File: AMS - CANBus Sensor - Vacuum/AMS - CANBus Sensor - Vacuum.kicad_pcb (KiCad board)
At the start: 2 copper layers, 72.9 x 71.1 mm, 45 parts, among them IC2 OPA4340UA, J1 Power_And_CAN, J2 Power_And_CAN, J3 TTL_Programmer, J4 ICSP, J5 Conn_01x02, J6 Screw_Terminal_01x02, Q1 IRF9Z34NPBF, U1 3568, U2 ATmega328P-P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

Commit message: wip for the vacuum
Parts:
- removed J2: Power_And_CAN, TerminalBlock_Phoenix:TerminalBlock_Phoenix_MPT-0,5-4-2.54_1x04_P2.54mm_Horizontal
- removed J6: Screw_Terminal_01x02, TerminalBlock_Phoenix:TerminalBlock_Phoenix_MPT-0,5-2-2.54_1x02_P2.54mm_Horizontal
- removed R12, R13: 47K, Resistor_SMD:R_1206_3216Metric_Pad1.30x1.75mm_HandSolder
- removed R14, R15, R8: 100K, Resistor_SMD:R_1206_3216Metric_Pad1.30x1.75mm_HandSolder
- removed RV1, RV2, RV3, RV4: 200k, Potentiometer_THT:Potentiometer_Bourns_3296W_Vertical
- IC2: value OPA4340UA -> MCP1804T-A002I_OT; footprint SamacSys_Parts:SOIC127P600X175-14N -> SamacSys_Parts:SOT95P270X145-5N
- R9: value 100K -> 1k; footprint Resistor_SMD:R_1206_3216Metric_Pad1.30x1.75mm_HandSolder -> Resistor_SMD:R_0603_1608Metric
- U1: value 3568 -> TL431LP; footprint SamacSys_Parts:3568 -> Package_TO_SOT_THT:TO-92_Inline
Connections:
- IC2 pad 1: /BareMinAtmel328P/PC1-A1 -> +VDC
- IC2 pad 2: /BareMinAtmel328P/PC1-A1 -> GND
- IC2 pad 3: /BufferedADC/ADCIN1 -> unconnected-(IC2-NC-Pad3)
- IC2 pad 4: +5V -> +VDC
- IC2 pad 5: /BufferedADC/ADCIN2 -> +10V
- R9 pad 1: GND -> +5V
- R9 pad 2: /BufferedADC/ADCIN2 -> +2V5
- U1 pad 1: Net-(J6-Pin_2) -> +2V5
- U1 pad 2: Net-(J6-Pin_1) -> GND
- U1 pad 3: +5V -> +2V5
- U2 pad 24: /BareMinAtmel328P/PC1-A1 -> +2V5
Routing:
- net GND: track 276.6 -> 0.00 mm, vias 2 -> 0
- net +5V: track 185.4 -> 0.00 mm, vias 2 -> 0
- net /BufferedADC/ADCIN4: track 98.9 -> 0.00 mm, vias 1 -> 0
- net /BareMinAtmel328P/PB3-D11-MOSI: track 98.5 -> 0.00 mm, vias 1 -> 0
- net /BareMinAtmel328P/PB1-D9: track 92.8 -> 0.00 mm, vias 2 -> 0
- net /BareMinAtmel328P/RESET: track 92.4 -> 0.00 mm, vias 4 -> 0
- net /BareMinAtmel328P/PC3-A3: track 78.5 -> 0.00 mm, vias 2 -> 0
- net Net-(U3-OSC1): track 77.0 -> 0.00 mm
- net /BareMinAtmel328P/PB5-D13-SCK: track 75.2 -> 0.00 mm, vias 2 -> 0
- net Net-(U3-OSC2): track 72.5 -> 0.00 mm
- net /BufferedADC/ADCIN3: track 58.3 -> 0.00 mm, vias 1 -> 0
- net /BareMinAtmel328P/PB4-D12-MISO: track 53.7 -> 0.00 mm, vias 2 -> 0
- net /BareMinAtmel328P/PC1-A1: track 51.2 -> 0.00 mm, vias 2 -> 0
- net /BareMinAtmel328P/PC2-A2: track 46.0 -> 0.00 mm, vias 3 -> 0
- net /BufferedADC/ADCIN2: track 45.2 -> 0.00 mm, vias 2 -> 0
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
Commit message: i think the Vacuum sensor is done i need to test s afew things and then this is ready for fab
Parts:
- removed R10, R11: 47K, Resistor_SMD:R_1206_3216Metric_Pad1.30x1.75mm_HandSolder
- added IC1: OPA2340UA_2K5, SamacSys_Parts:SOIC127P600X175-8N, B.Cu at (121.3, 102.7)
- added IC3: ADS1115IDGST, SamacSys_Parts:SOP50P490X110-10N, B.Cu at (153.9, 93.6)
- added IC4: 24PCDFA6D, SamacSys_Parts:24PCDFA6D, F.Cu at (159.3, 88.8)
- added IC6: 24PCDFA6D, SamacSys_Parts:24PCDFA6D, F.Cu at (159.3, 103.6)
- added IC8: INA849DR, SamacSys_Parts:SOIC127P600X175-8N, B.Cu at (167.4, 84.9)
- added IC9: INA849DR, SamacSys_Parts:SOIC127P600X175-8N, B.Cu at (167.6, 99.8)
- added R12: 10k, Resistor_SMD:R_1206_3216Metric_Pad1.30x1.75mm_HandSolder, B.Cu at (144.8, 86.9)
- added R13: 10k, Resistor_SMD:R_1206_3216Metric_Pad1.30x1.75mm_HandSolder, B.Cu at (144.8, 83.3)
- added R14: YR1B665RCC, SamacSys_Parts:RESAD1550W60L630D230, F.Cu at (163.0, 79.6)
- added R15: YR1B665RCC, SamacSys_Parts:RESAD1550W60L630D230, F.Cu at (163.0, 105.7)
- added R16: 120k, Resistor_SMD:R_1206_3216Metric_Pad1.30x1.75mm_HandSolder, F.Cu at (124.0, 101.5)
- added R17: 15k, Resistor_SMD:R_1206_3216Metric_Pad1.30x1.75mm_HandSolder, F.Cu at (129.1, 101.4)
- added R18: 47k, Resistor_SMD:R_1206_3216Metric_Pad1.30x1.75mm_HandSolder, F.Cu at (117.1, 101.8)
- added R19: 1M, Resistor_SMD:R_1206_3216Metric_Pad1.30x1.75mm_HandSolder, F.Cu at (117.1, 105.5)
- added R8: 10k, Resistor_SMD:R_1206_3216Metric_Pad1.30x1.75mm_HandSolder, B.Cu at (163.3, 92.6)
- moved R6 33.3 mm to (138.2, 59.5), turned to -90 degrees
- moved U4 24.5 mm to (143.9, 60.9), turned to -90 degrees
- moved J5 18.3 mm to (157.3, 62.6)
- moved R7 18.3 mm to (157.4, 59.1)
- moved D1 14.2 mm to (169.3, 70.1), turned to 0 degrees
- moved U1 13.7 mm to (169.8, 111.6)
- moved Q1 12.8 mm to (142.7, 73.2)
- moved R5 10.8 mm to (135.5, 80.1)
- moved U3 6.09 mm to (151.8, 73.7)
- moved J4 6.01 mm to (151.8, 71.1)
- moved J1 5.72 mm to (161.9, 75.1)
- moved C2 2.19 mm to (154.2, 115.6)
- moved C3 2.19 mm to (154.2, 115.6)
- moved C4 2.19 mm to (159.6, 115.5)
- moved Y1 2.19 mm to (154.6, 119.7)
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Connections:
- U2 pad 24: +2V5 -> /BareMinAtmel328P/PC1-A1
- U2 pad 27: /BareMinAtmel328P/PC4-A4-SDA -> /SDAB
- U2 pad 28: /BareMinAtmel328P/PC5-A5-SCL -> /SCLB
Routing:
- net GND: track 0.00 -> 284.1 mm, vias 0 -> 2
- net +5V: track 0.00 -> 194.1 mm, vias 0 -> 4
- net /ADS1115/AIN0: track 0.00 -> 83.4 mm, vias 0 -> 3
- net /BareMinAtmel328P/RESET: track 0.00 -> 66.6 mm, vias 0 -> 2
- net +10V: track 0.00 -> 59.3 mm, vias 0 -> 1
- net +2V5: track 0.00 -> 57.9 mm, vias 0 -> 1
- net /BareMinAtmel328P/PB1-D9: track 0.00 -> 52.2 mm, vias 0 -> 2
- net /BareMinAtmel328P/PB4-D12-MISO: track 0.00 -> 48.8 mm, vias 0 -> 3
- net /BareMinAtmel328P/PB3-D11-MOSI: track 0.00 -> 48.2 mm, vias 0 -> 3
- net /ADS1115/AIN3: track 0.00 -> 46.0 mm, vias 0 -> 2
- net +VDC: track 0.00 -> 45.3 mm, vias 0 -> 2
- net Net-(U3-OSC2): track 0.00 -> 44.2 mm, vias 0 -> 3
- net Net-(U3-OSC1): track 0.00 -> 43.5 mm, vias 0 -> 2
- net /BareMinAtmel328P/PB5-D13-SCK: track 0.00 -> 43.3 mm, vias 0 -> 3
- net /BareMinAtmel328P/PD1-TX: track 0.00 -> 39.9 mm
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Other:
- board text added: "AMS CANBus Vacuum V1.0 Rev A"
- board text added: "PORT1"
- board text added: "PORT2"
- board text removed: "1 Amp 5V"
- board text removed: "ADC"
- board text removed: "AMS CANBus Voltage V1.0 Rev A"
- board text removed: "Fused"
- board text removed: "In"
- board text removed: "In 1"
- board text removed: "In 2"
- board text removed: "In 3"
- board text removed: "In 4"

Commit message: vacuum wip
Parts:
- added C10: 22nF, Capacitor_SMD:C_1206_3216Metric_Pad1.33x1.80mm_HandSolder, B.Cu at (169.6, 108.3)
- added C11: 1uF, Capacitor_SMD:C_0603_1608Metric_Pad1.08x0.95mm_HandSolder, B.Cu at (124.9, 97.3)
- added C8: 10uF, Capacitor_SMD:C_0603_1608Metric_Pad1.08x0.95mm_HandSolder, B.Cu at (122.0, 89.8)
- added C9: 22uF, Capacitor_SMD:C_0603_1608Metric_Pad1.08x0.95mm_HandSolder, F.Cu at (126.1, 89.8)
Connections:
- U2 pad 5: /BareMinAtmel328P/PD3-D3 -> /ADS1115/Alert/Ready
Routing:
- net GND: track 284.1 -> 298.3 mm
- net +2V5: track 57.9 -> 61.9 mm
- net +5V: track 194.1 -> 196.7 mm
- net +VDC: track 45.3 -> 47.0 mm

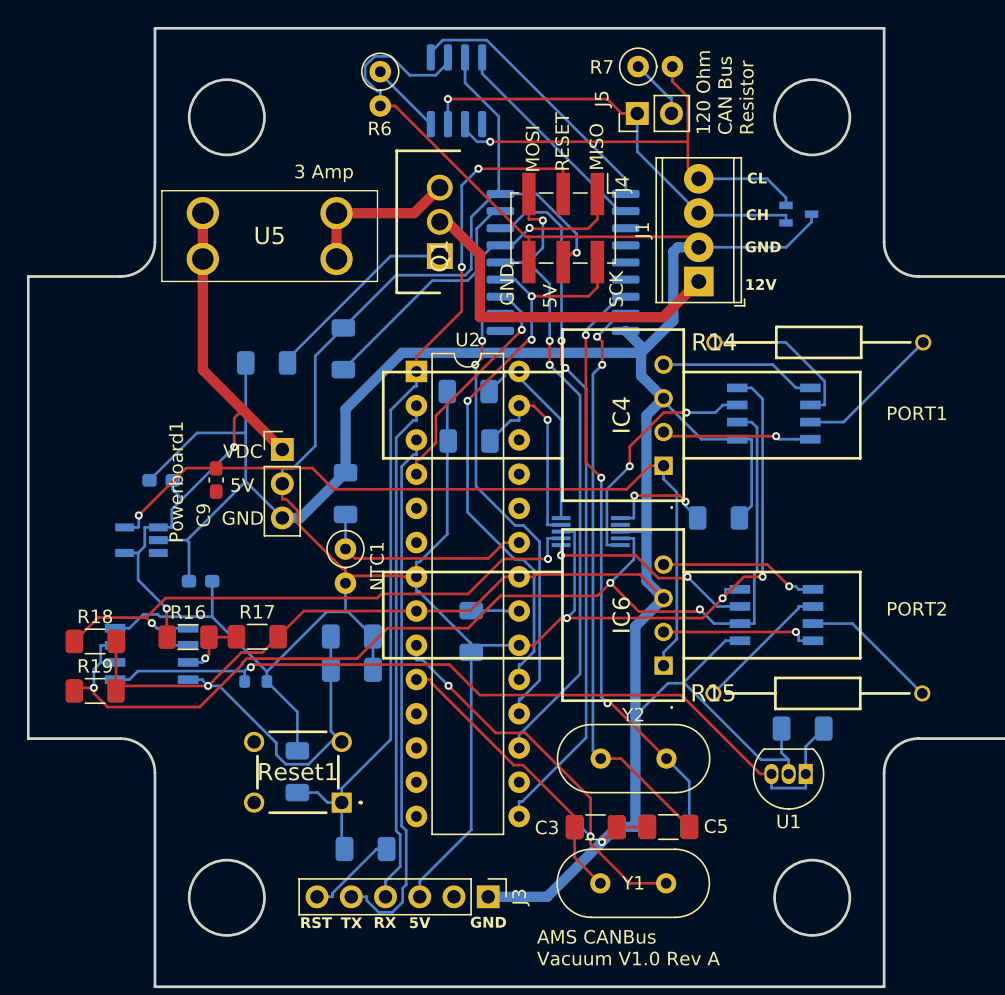
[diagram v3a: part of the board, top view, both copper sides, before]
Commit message: flipped the powerboard input to match the designs i have.
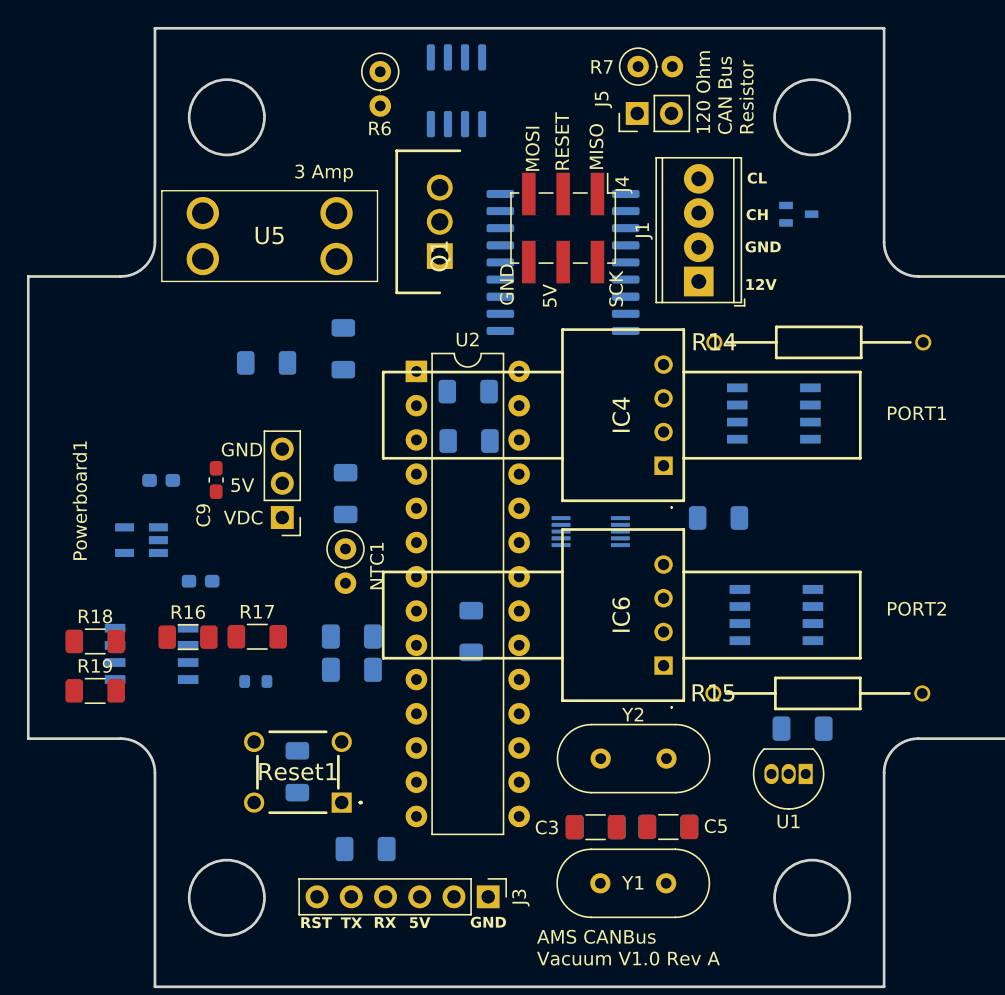
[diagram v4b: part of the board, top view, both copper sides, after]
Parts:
- moved Powerboard1 5.05 mm to (131.0, 92.6), turned to 180 degrees
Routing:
- net GND: track 298.3 -> 0.00 mm, vias 2 -> 0
- net +5V: track 196.7 -> 0.00 mm, vias 4 -> 0
- net /ADS1115/AIN0: track 83.4 -> 0.00 mm, vias 3 -> 0
- net /BareMinAtmel328P/RESET: track 66.6 -> 0.00 mm, vias 2 -> 0
- net +2V5: track 61.9 -> 0.00 mm, vias 1 -> 0
- net +10V: track 59.3 -> 0.00 mm, vias 1 -> 0
- net /BareMinAtmel328P/PB1-D9: track 52.2 -> 0.00 mm, vias 2 -> 0
- net /BareMinAtmel328P/PB4-D12-MISO: track 48.8 -> 0.00 mm, vias 3 -> 0
- net /BareMinAtmel328P/PB3-D11-MOSI: track 48.2 -> 0.00 mm, vias 3 -> 0
- net +VDC: track 47.0 -> 0.00 mm, vias 2 -> 0
- net /ADS1115/AIN3: track 46.0 -> 0.00 mm, vias 2 -> 0
- net Net-(U3-OSC2): track 44.2 -> 0.00 mm, vias 3 -> 0
- net Net-(U3-OSC1): track 43.5 -> 0.00 mm, vias 2 -> 0
- net /BareMinAtmel328P/PB5-D13-SCK: track 43.3 -> 0.00 mm, vias 3 -> 0
- net /BareMinAtmel328P/PD1-TX: track 39.9 -> 0.00 mm
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
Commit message: clean up and start of the work for the PCB
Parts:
- removed IC1: OPA2340UA_2K5, SamacSys_Parts:SOIC127P600X175-8N
- removed R16: 120k, Resistor_SMD:R_1206_3216Metric_Pad1.30x1.75mm_HandSolder
- removed R17: 15k, Resistor_SMD:R_1206_3216Metric_Pad1.30x1.75mm_HandSolder
- removed R18: 47k, Resistor_SMD:R_1206_3216Metric_Pad1.30x1.75mm_HandSolder
- removed R19: 1M, Resistor_SMD:R_1206_3216Metric_Pad1.30x1.75mm_HandSolder
- removed R9: 1k, Resistor_SMD:R_0603_1608Metric
- removed U1: TL431LP, Package_TO_SOT_THT:TO-92_Inline
- added C12: 100pF, Capacitor_SMD:C_0603_1608Metric_Pad1.08x0.95mm_HandSolder, F.Cu at (97.9, 49.8)
- added C13: 0.1uF, Capacitor_SMD:C_0603_1608Metric_Pad1.08x0.95mm_HandSolder, F.Cu at (97.9, 52.3)
- added C14: 120uF, Capacitor_THT:CP_Radial_D8.0mm_P5.00mm, F.Cu at (75.0, 47.8)
- added C15: 0.1uF, Capacitor_SMD:C_0603_1608Metric_Pad1.08x0.95mm_HandSolder, F.Cu at (97.9, 54.8)
- added C16: 68uF, Capacitor_THT:CP_Radial_D8.0mm_P5.00mm, F.Cu at (64.4, 48.0)
- added D2: 1N5817, SamacSys_Parts:DIOAD1414W86L464D238, F.Cu at (87.0, 41.6)
- added IC5: MAX764CPA+, SamacSys_Parts:DIP762W56P254L938H457Q8N, F.Cu at (90.6, 54.3)
- added L1: 47uH, Inductor_THT:L_Axial_L7.0mm_D3.3mm_P10.16mm_Horizontal_Fastron_MICC, F.Cu at (87.0, 46.1)
- C10: value 22nF -> 100pF; footprint Capacitor_SMD:C_1206_3216Metric_Pad1.33x1.80mm_HandSolder -> Capacitor_SMD:C_0603_1608Metric_Pad1.08x0.95mm_HandSolder
- moved IC4 60.9 mm to (218.3, 73.6)
- moved IC8 60.9 mm to (226.4, 69.8)
- moved IC9 55.9 mm to (223.2, 93.4)
- moved IC6 55.9 mm to (214.8, 97.1)
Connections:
- C10 pad 1: +2V5 -> GND
- IC3 pad 5: /ADS1115/AIN1 -> GND
- IC3 pad 7: /ADS1115/AIN3 -> GND
- IC8 pad 5: GND -> -5V
- IC8 pad 6: /ADS1115/AIN0 -> GND
- IC8 pad 7: /ADS1115/AIN1 -> /ADS1115/AIN0
- IC9 pad 5: GND -> -5V
- IC9 pad 6: /ADS1115/AIN0 -> GND
